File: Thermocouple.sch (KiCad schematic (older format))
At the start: 0 parts

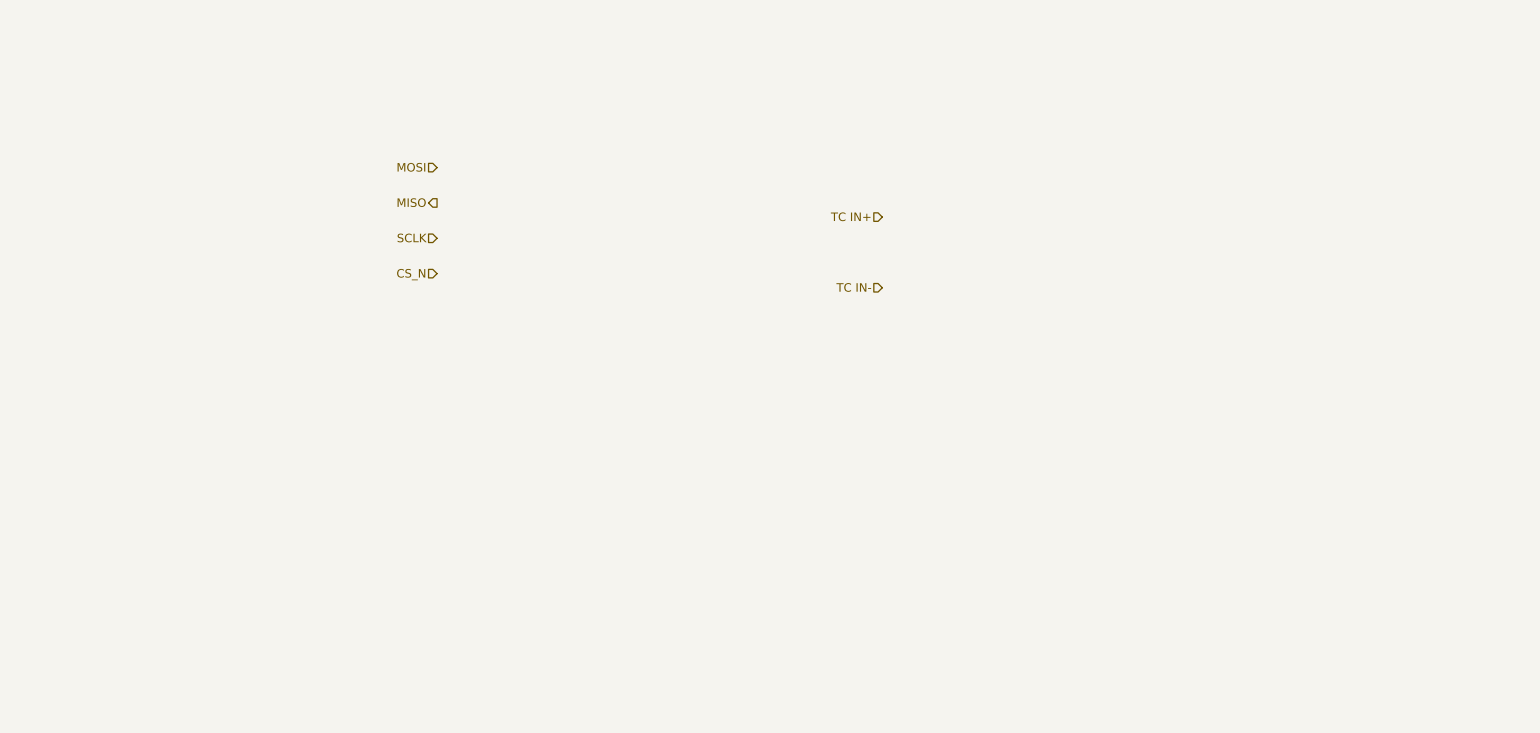
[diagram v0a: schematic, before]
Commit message: Added Powercontrol stuff
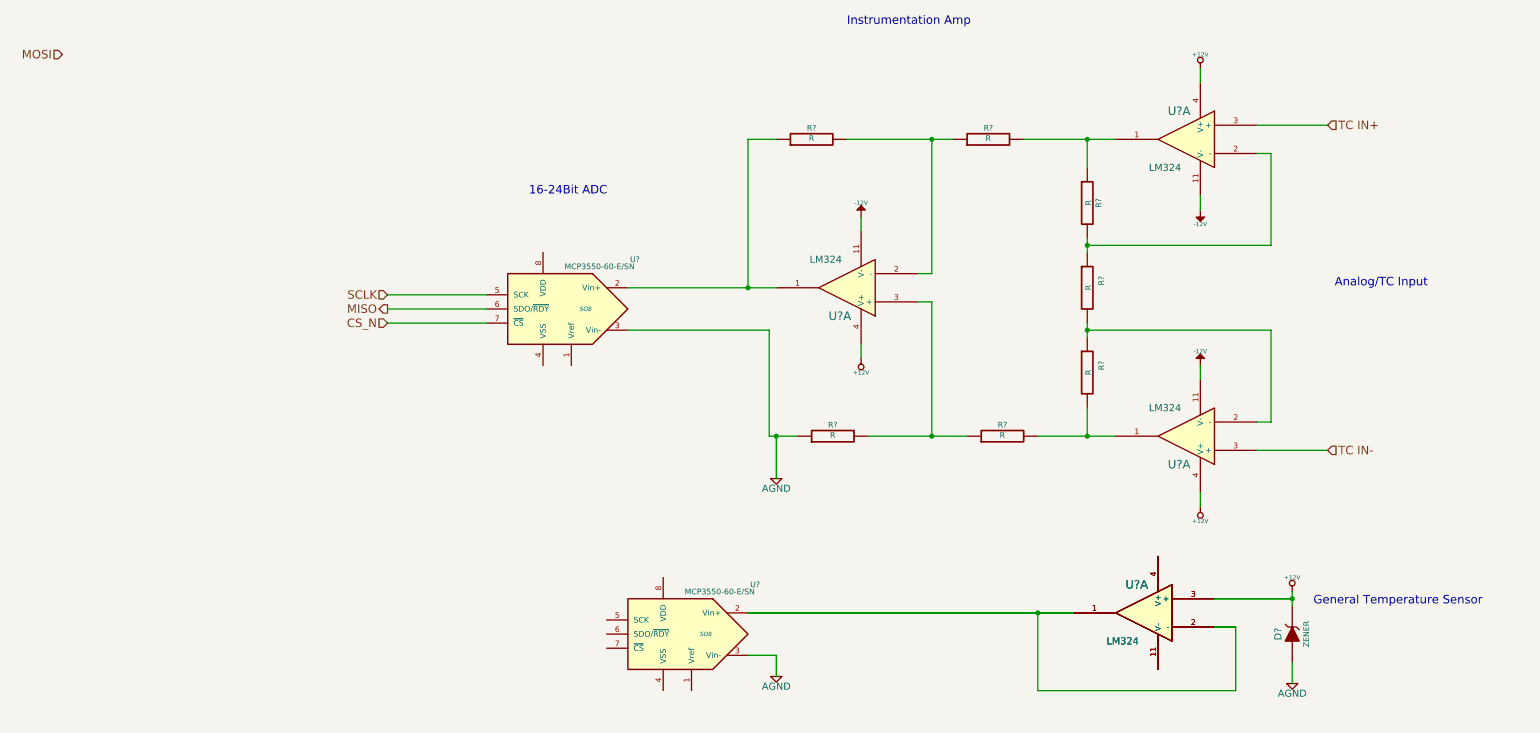
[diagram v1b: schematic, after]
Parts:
- added D?: ZENER, ~, symbol ZENER
- added R? (x7): R, ~, symbol R
- added U? (x5): LM324, symbol LM324
- added U? (x2): MCP3550-60-E/SN, SO8, symbol MCP3550-60-E/SN
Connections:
- net CS_N: now also U?.7 (~CS~)
- net MISO: now also U?.6 (SDO/~RDY~)
- net SCLK: now also U?.5 (SCK)
- net TC IN+: now also U?.3 (+)
- net TC IN-: now also U?.3 (+)
- new net: R?.1, R?.2, U?.1
- new net: R?.1, R?.2, U?.2 (-) (x3)
- new net: R?.2, R?.2, U?.1
- new net: R?.1, U?.1, U?.2 (Vin+)
- new net: R?.1, R?.2, U?.3 (+)
- new net: U?.1, U?.1, U?.2 (-), U?.2 (-), U?.2 (Vin+)
- new net: U?.11 (V-), U?.11 (V-)
- new net: U?.4 (V+), U?.4 (V+)
- new net +12V: D?.2 (K), U?.3 (+), U?.3 (+), U?.4 (V+), U?.4 (V+), U?.4 (V+)
- new net -12V: U?.11 (V-), U?.11 (V-), U?.11 (V-)
- new net AGND: D?.1 (A), R?.1, U?.3 (Vin-), U?.3 (Vin-)
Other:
- note added: "16-24Bit ADC"
- note added: "Analog/TC Input\n"
- note added: "General Temperature Sensor\n"
- note added: "Instrumentation Amp\n"

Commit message: Nach Einfuegen Relay-Modul
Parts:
- gave numbers to parts that had none: 12
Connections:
- net +12V: now also U4.10 (+), U4.5 (+); no longer U4.3 (+), U4.3 (+)
- net TC IN+: now also U4.12 (+); no longer U4.3 (+)
- net at R11.1, R9.2: now also U4.14; no longer U4.1
- net at R11.2, R12.1: now also U4.13 (-); no longer U4.2 (-)
- new net: U3.2 (Vin+), U4.6 (-), U4.7, U4.8, U4.9 (-)
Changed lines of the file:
@@
 Sheet 3 9
 Title ""
-Date "14 feb 2014"
+Date "17 feb 2014"
 Rev ""
 Comp ""
@@
 CS_N
 $Comp
-L LM324 U?
-U 1 1 52EFE353
+L LM324 U4
+U 4 1 52EFE353
 P 8950 2100
-F 0 "U?" H 9000 2300 60  0000 C CNN
+F 0 "U4" H 9000 2300 60  0000 C CNN
 F 1 "LM324" H 9100 1900 50  0000 C CNN
 F 2 "" H 8950 2100 60  0000 C CNN
 F 3 "" H 8950 2100 60  0000 C CNN
-	1    8950 2100
+	4    8950 2100
 	-1   0    0    -1
 $EndComp
 $Comp
-L LM324 U?
+L LM324 U5
 U 1 1 52EFE36F
 P 8950 4200
-F 0 "U?" H 9000 4400 60  0000 C CNN
+F 0 "U5" H 9000 4400 60  0000 C CNN
 F 1 "LM324" H 9100 4000 50  0000 C CNN
 F 2 "" H 8950 4200 60  0000 C CNN
@@
 $EndComp
 $Comp
-L LM324 U?
+L LM324 U4
 U 1 1 52EFE375
 P 6550 3150
-F 0 "U?" H 6600 3350 60  0000 C CNN
+F 0 "U4" H 6600 3350 60  0000 C CNN
 F 1 "LM324" H 6700 2950 50  0000 C CNN
 F 2 "" H 6550 3150 60  0000 C CNN
@@
 $EndComp
 $Comp
-L R R?
+L R R12
 U 1 1 52EFE44C
 P 8250 3150
-F 0 "R?" V 8350 3200 40  0000 C CNN
+F 0 "R12" V 8350 3200 40  0000 C CNN
 F 1 "R" V 8257 3151 40  0000 C CNN
 F 2 "~" V 8180 3150 30  0000 C CNN
@@
 $EndComp
 $Comp
-L R R?
+L R R11
 U 1 1 52EFE459
 P 8250 2550
-F 0 "R?" V 8330 2550 40  0000 C CNN
+F 0 "R11" V 8330 2550 40  0000 C CNN
 F 1 "R" V 8257 2551 40  0000 C CNN
 F 2 "~" V 8180 2550 30  0000 C CNN
@@
 $EndComp
 $Comp
-L R R?
+L R R13
 U 1 1 52EFE473
 P 8250 3750
-F 0 "R?" V 8350 3800 40  0000 C CNN
+F 0 "R13" V 8350 3800 40  0000 C CNN
 F 1 "R" V 8257 3751 40  0000 C CNN
 F 2 "~" V 8180 3750 30  0000 C CNN
@@
 	7900 4200 8450 4200
 $Comp
-L R R?
+L R R9
 U 1 1 52EFE4C4
 P 7550 2100
-F 0 "R?" V 7630 2100 40  0000 C CNN
+F 0 "R9" V 7630 2100 40  0000 C CNN
 F 1 "R" V 7557 2101 40  0000 C CNN
 F 2 "~" V 7480 2100 30  0000 C CNN
@@
 $EndComp
 $Comp
-L R R?
+L R R10
 U 1 1 52EFE4E0
 P 7650 4200
-F 0 "R?" V 7730 4200 40  0000 C CNN
+F 0 "R10" V 7730 4200 40  0000 C CNN
 F 1 "R" V 7657 4201 40  0000 C CNN
 F 2 "~" V 7580 4200 30  0000 C CNN
@@
 $EndComp
 $Comp
-L R R?
+L R R7
 U 1 1 52EFE507
 P 6300 2100
-F 0 "R?" V 6380 2100 40  0000 C CNN
+F 0 "R7" V 6380 2100 40  0000 C CNN
 F 1 "R" V 6307 2101 40  0000 C CNN
 F 2 "~" V 6230 2100 30  0000 C CNN
@@
 $EndComp
 $Comp
-L R R?
+L R R8
 U 1 1 52EFE51E
 P 6450 4200
-F 0 "R?" V 6530 4200 40  0000 C CNN
+F 0 "R8" V 6530 4200 40  0000 C CNN
 F 1 "R" V 6457 4201 40  0000 C CNN
 F 2 "~" V 6380 4200 30  0000 C CNN
@@
 	9950 4300 9450 4300
 $Comp
-L +12V #PWR?
+L +12V #PWR4
 U 1 1 52EFE7A2
 P 6650 3650
-F 0 "#PWR?" H 6650 3600 20  0001 C CNN
+F 0 "#PWR4" H 6650 3600 20  0001 C CNN
 F 1 "+12V" H 6650 3750 30  0000 C CNN
 F 2 "" H 6650 3650 60  0000 C CNN
@@
 $EndComp
 $Comp
-L +12V #PWR?
+L +12V #PWR5
 U 1 1 52EFE7AF
 P 9050 1600
-F 0 "#PWR?" H 9050 1550 20  0001 C CNN
+F 0 "#PWR5" H 9050 1550 20  0001 C CNN
 F 1 "+12V" H 9050 1700 30  0000 C CNN
 F 2 "" H 9050 1600 60  0000 C CNN
@@
 $EndComp
 $Comp
-L +12V #PWR?
+L +12V #PWR8
 U 1 1 52EFE8B9
 P 9050 4700
-F 0 "#PWR?" H 9050 4650 20  0001 C CNN
+F 0 "#PWR8" H 9050 4650 20  0001 C CNN
 F 1 "+12V" H 9050 4800 30  0000 C CNN
 F 2 "" H 9050 4700 60  0000 C CNN
@@
 $EndComp
 $Comp
-L -12V #PWR?
+L -12V #PWR7
 U 1 1 52EFE8DC
 P 9050 3700
-F 0 "#PWR?" H 9050 3830 20  0001 C CNN
+F 0 "#PWR7" H 9050 3830 20  0001 C CNN
 F 1 "-12V" H 9050 3800 30  0000 C CNN
 F 2 "" H 9050 3700 60  0000 C CNN
@@
 $EndComp
 $Comp
-L -12V #PWR?
+L -12V #PWR6
 U 1 1 52EFE8EB
 P 9050 2600
-F 0 "#PWR?" H 9050 2730 20  0001 C CNN
+F 0 "#PWR6" H 9050 2730 20  0001 C CNN
 F 1 "-12V" H 9050 2700 30  0000 C CNN
 F 2 "" H 9050 2600 60  0000 C CNN
@@
 $EndComp
 $Comp
-L -12V #PWR?
+L -12V #PWR3
 U 1 1 52EFE908
 P 6650 2650
-F 0 "#PWR?" H 6650 2780 20  0001 C CNN
+F 0 "#PWR3" H 6650 2780 20  0001 C CNN
 F 1 "-12V" H 6650 2750 30  0000 C CNN
 F 2 "" H 6650 2650 60  0000 C CNN
@@
 	6650 3650 6650 3550
 $Comp
-L AGND #PWR?
+L AGND #PWR1
 U 1 1 52EFE9F3
 P 6050 4500
-F 0 "#PWR?" H 6050 4500 40  0001 C CNN
+F 0 "#PWR1" H 6050 4500 40  0001 C CNN
 F 1 "AGND" H 6050 4430 50  0000 C CNN
 F 2 "" H 6050 4500 60  0000 C CNN
@@
 	6050 4200 6050 4500
 $Comp
-L MCP3550-60-E/SN U?
+L MCP3550-60-E/SN U2
 U 1 1 52EFEA95
 P 4500 3300
-F 0 "U?" H 3950 3650 40  0000 C CNN
+F 0 "U2" H 3950 3650 40  0000 C CNN
 F 1 "MCP3550-60-E/SN" H 4200 3600 40  0000 C CNN
 F 2 "SO8" H 4300 3300 30  0000 C CIN
@@
 	3300 3400 4000 3400
 $Comp
-L MCP3550-60-E/SN U?
+L MCP3550-60-E/SN U3
 U 1 1 52EFEBA0
 P 5350 5600
-F 0 "U?" H 4800 5950 40  0000 C CNN
+F 0 "U3" H 4800 5950 40  0000 C CNN
 F 1 "MCP3550-60-E/SN" H 5050 5900 40  0000 C CNN
 F 2 "SO8" H 5150 5600 30  0000 C CIN
@@
 $EndComp
 $Comp
-L LM324 U?
-U 1 1 52EFEBA6
+L LM324 U4
+U 2 1 52EFEBA6
 P 8650 5450
-F 0 "U?" H 8700 5650 60  0000 C CNN
+F 0 "U4" H 8700 5650 60  0000 C CNN
 F 1 "LM324" H 8800 5250 50  0000 C CNN
 F 2 "" H 8650 5450 60  0000 C CNN
 F 3 "" H 8650 5450 60  0000 C CNN
-	1    8650 5450
+	2    8650 5450
 	-1   0    0    -1
 $EndComp
 $Comp
-L ZENER D?
+L ZENER D3
 U 1 1 52EFEBDB
 P 9700 5600
-F 0 "D?" H 9700 5700 50  0000 C CNN
+F 0 "D3" H 9700 5700 50  0000 C CNN
 F 1 "ZENER" H 9700 5500 40  0000 C CNN
 F 2 "~" H 9700 5600 60  0000 C CNN
@@
 $EndComp
 $Comp
-L AGND #PWR?
+L AGND #PWR10
 U 1 1 52EFEC29
 P 9700 5950
-F 0 "#PWR?" H 9700 5950 40  0001 C CNN
+F 0 "#PWR10" H 9700 5950 40  0001 C CNN
 F 1 "AGND" H 9700 5880 50  0000 C CNN
 F 2 "" H 9700 5950 60  0000 C CNN
@@
 $EndComp
 $Comp
-L +12V #PWR?
+L +12V #PWR9
 U 1 1 52EFEC47
 P 9700 5300
-F 0 "#PWR?" H 9700 5250 20  0001 C CNN
+F 0 "#PWR9" H 9700 5250 20  0001 C CNN
 F 1 "+12V" H 9700 5400 30  0000 C CNN
 F 2 "" H 9700 5300 60  0000 C CNN
@@
 Connection ~ 7900 5450
 $Comp
-L AGND #PWR?
+L AGND #PWR2
 U 1 1 52EFEE3B
 P 6050 5900
-F 0 "#PWR?" H 6050 5900 40  0001 C CNN
+F 0 "#PWR2" H 6050 5900 40  0001 C CNN
 F 1 "AGND" H 6050 5830 50  0000 C CNN
 F 2 "" H 6050 5900 60  0000 C CNN
@@
 Analog/TC Input\n
 $Comp
-L LM324 U?
-U 1 1 52F140F0
+L LM324 U4
+U 3 1 52F140F0
 P 8650 5450
-F 0 "U?" H 8700 5650 60  0000 C CNN
+F 0 "U4" H 8700 5650 60  0000 C CNN
 F 1 "LM324" H 8800 5250 50  0000 C CNN
 F 2 "" H 8650 5450 60  0000 C CNN
 F 3 "" H 8650 5450 60  0000 C CNN
-	1    8650 5450
+	3    8650 5450
 	-1   0    0    -1
 $EndComp
-Wire Wire Line
-	9150 5350 9700 5350
-Wire Wire Line
-	9150 5550 9300 5550
-Wire Wire Line
-	5850 5450 8150 5450
 $EndSCHEMATC

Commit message: Am Ende der 5. Woche.
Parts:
- removed D3: ZENER, ~, symbol ZENER
- removed U2, U3: MCP3550-60-E/SN, SO8, symbol MCP3550-60-E/SN
- removed unit 2 of U4
- removed unit 3 of U4
- added C10, C11, C6, C7, C8, C9: C, ~, symbol C
- added P2: CONN_3X2, symbol CONN_3X2
- added P3: CONN_2, symbol CONN_2
- added R44, R45: R, ~, symbol R
- added R48, R49: 0, ~, symbol R
- added U2: MCP3901, symbol MCP3901
- added U3: LMT84, symbol LMT84
- U4: value LM324 -> OPA4170
- U4: renamed from U5; value LM324 -> OPA4170
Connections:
- net +12V: now also C10.2; no longer U4.4 (V+)
- net -12V: now also C9.2
- net AGND: now also C10.1, C6.2, C7.1, C8.2, C9.1, R48.1, R49.1, U2.11 (DGND), U2.8 (AGND), U3.1 (GND), U3.2 (GND), U3.5 (GND)
- net MISO: now also U2.19 (SDO)
- net MOSI: now also U2.20 (SDI)
- net SCLK: now also U2.18 (SCK)
- net TC IN+: now also U4.10 (+); no longer U4.12 (+)
- net TC IN-: now also U4.12 (+); no longer U4.3 (+)
- net at R11.1, R9.2: now also U4.8; no longer U4.14
- net at R10.2, R13.2: now also U4.14; no longer U4.1
- net at R12.2, R13.1: now also U4.13 (-), R44.2, R45.2; no longer U4.2 (-)
- net CH0+: now reaches R7.1, U4.1
- net CH0+: now also C6.1, U2.4 (CH0+)
- new net: P2.1, P2.3, P2.5, R11.2, U4.9 (-)
- new net: P2.6, R12.1
- new net: P3.1 (P1), U2.12 (MDAT1)
- new net: P3.2 (PM), U2.13 (MDAT0)
- new net: P2.4, R44.1
- new net: P2.2, R45.1
- new net +5V: C11.1, C7.2, C8.1, U2.2 (DVDD), U2.3 (AVDD), U3.4 (Vdd)
- new net CH0-: R49.2, U2.5 (CH0-)
- new net CH1+: U2.7 (CH1+), U3.3 (OUT)
- new net CH1-: R48.2, U2.6 (CH1-)
- new net REF+: U2.9 (REFIN/OUT+)
- new net REF-: U2.10 (REFIN-)
- new net ~CS: U2.17 (~CS)
- new net ~DR: U2.14 (~DR)
- new net ~RESET: U2.1 (~RESET)
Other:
- note added: "Temp Sensor\n"
- note removed: "General Temperature Sensor\n"
- moved on the sheet: R12
